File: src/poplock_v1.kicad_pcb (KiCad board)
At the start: 2 copper layers, 62 parts, among them IC1 L293D, P1 CONN_02X08, P10 CONN_02X06, P2 CONN_02X10, P3 12V Connector, P4 LOCK_CONNECTOR, P9 CONN_02X08, Q1 2n7000, Q2 2n7000, Q3 2n7000, SW1 SPST, U1 ESP-12E, U2 LD1117S50CTR, U3 LD1117S33CTR, U4 MIC_ELECTRET

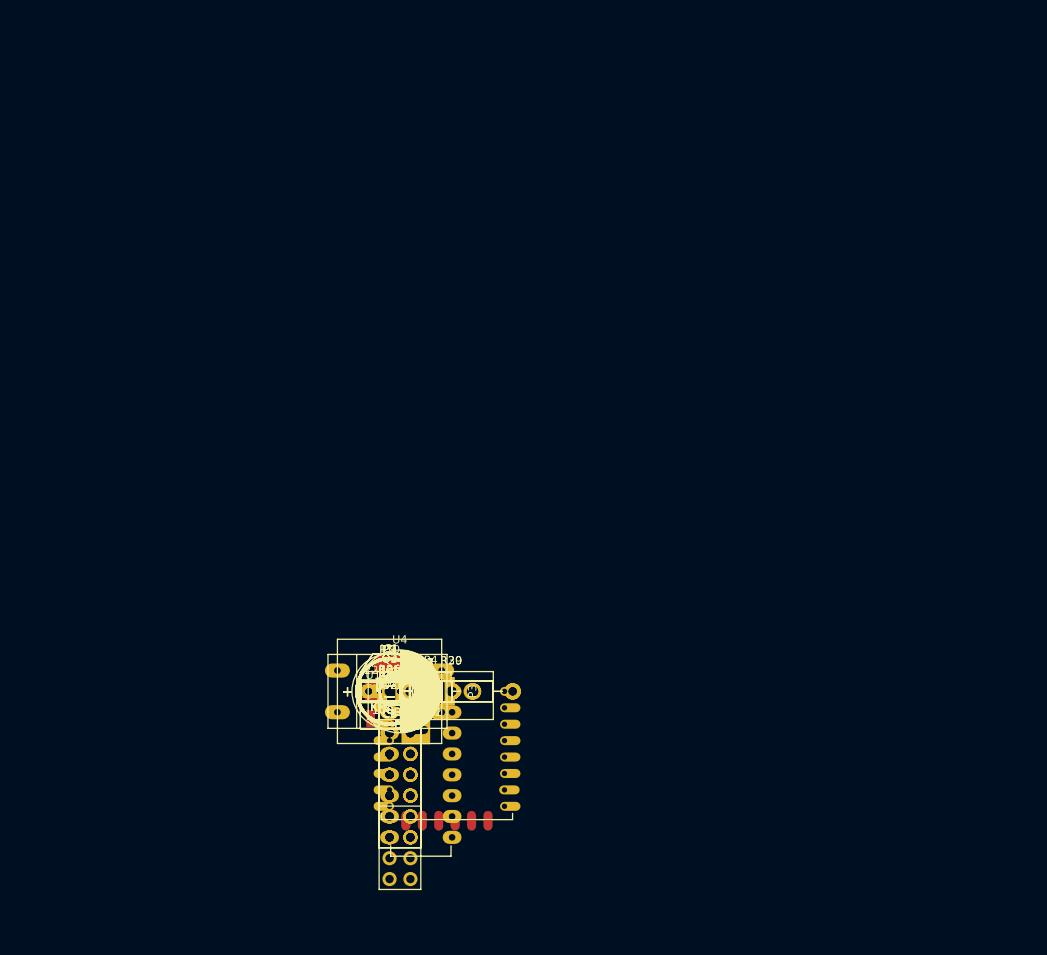
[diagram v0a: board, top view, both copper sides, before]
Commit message: Distribuidos os componentes sobre a placa.
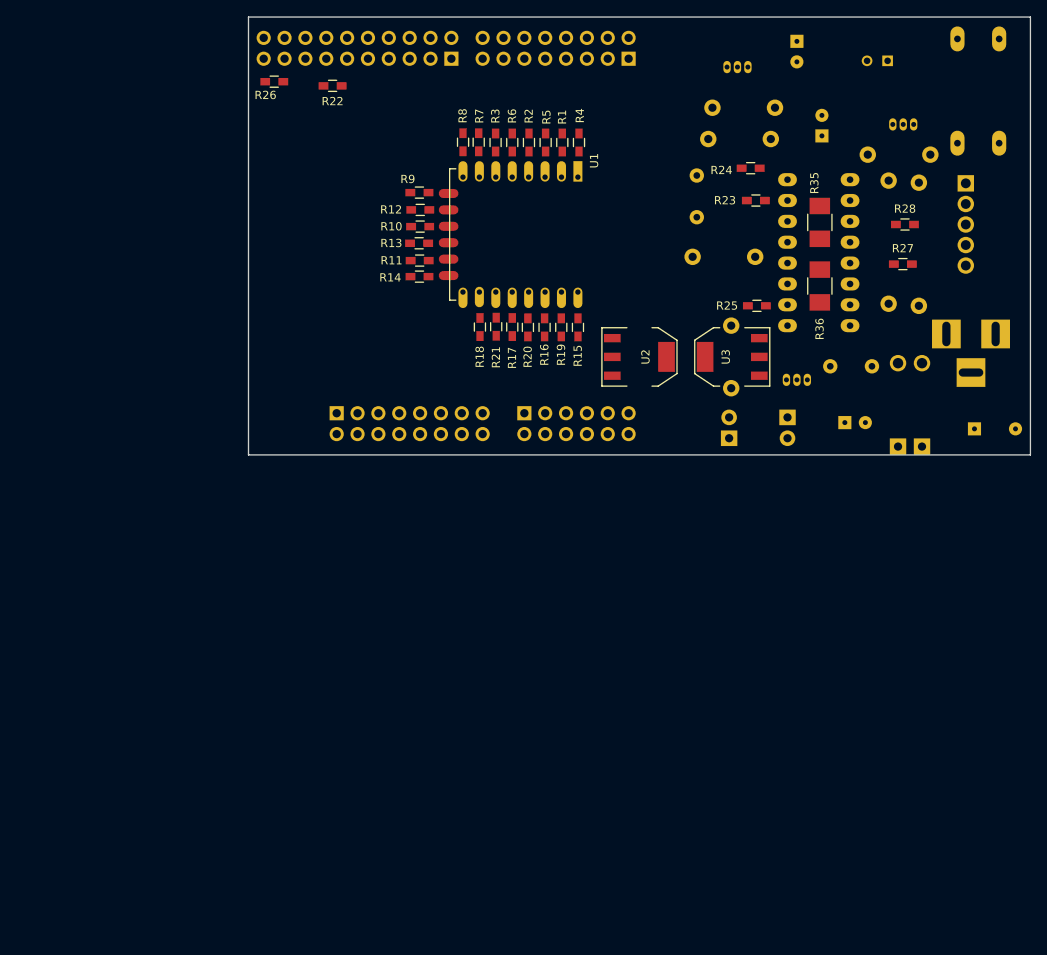
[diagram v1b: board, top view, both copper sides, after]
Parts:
- C1, C2, C3, C4, C5, C6, D1, D2, D3, D4, IC1, P1, P10, P2, P3, P9, Q1, Q2, Q3, R29, R30, R31, R32, R33, R34, R37, SW1, U4: moved to B.Cu
- P4: footprint Connect:Wafer_Vertical15x5.8x7RM2.5-5 -> Connect:Wafer_Horizontal15x5.8x7RM2.5-5; moved to B.Cu
- moved SW1 102.4 mm to (220.2, 31.9), turned to 90 degrees
- moved U4 97.9 mm to (209.2, 28.2), turned to 180 degrees
- moved Q3 94.1 mm to (212.3, 35.9), turned to 180 degrees
- moved P4 93.6 mm to (218.7, 43.1), turned to 270 degrees
- moved C6 92.4 mm to (198.1, 27.1), turned to 270 degrees
- moved R30 89.4 mm to (213.0, 43.0), turned to 270 degrees
- moved Q1 87.7 mm to (192.2, 29.0), turned to 180 degrees
- moved R33 87.6 mm to (206.8, 39.6)
- moved C3 86.7 mm to (201.2, 36.1), turned to 90 degrees
- moved P3 85.9 mm to (222.5, 61.5), turned to 180 degrees
- moved R28 84.7 mm to (211.3, 48.1)
- moved IC1 83.9 mm to (204.6, 42.7), turned to 180 degrees
- moved P1 82.4 mm to (177.6, 27.9), turned to 90 degrees
- moved R34 81.8 mm to (194.9, 37.7), turned to 180 degrees
- moved R27 81.4 mm to (211.0, 53.0)
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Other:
- board outline added: 95.2 x 53.3 mm
- net class Default: clearance 0.2 -> 0.4; trace_width 0.25 -> 0.4
- net class Power12 added: clearance 0.4, trace_width 0.4, via_dia 0.6, via_drill 0.4
- rule trace_clearance: 0.2 -> 0.4

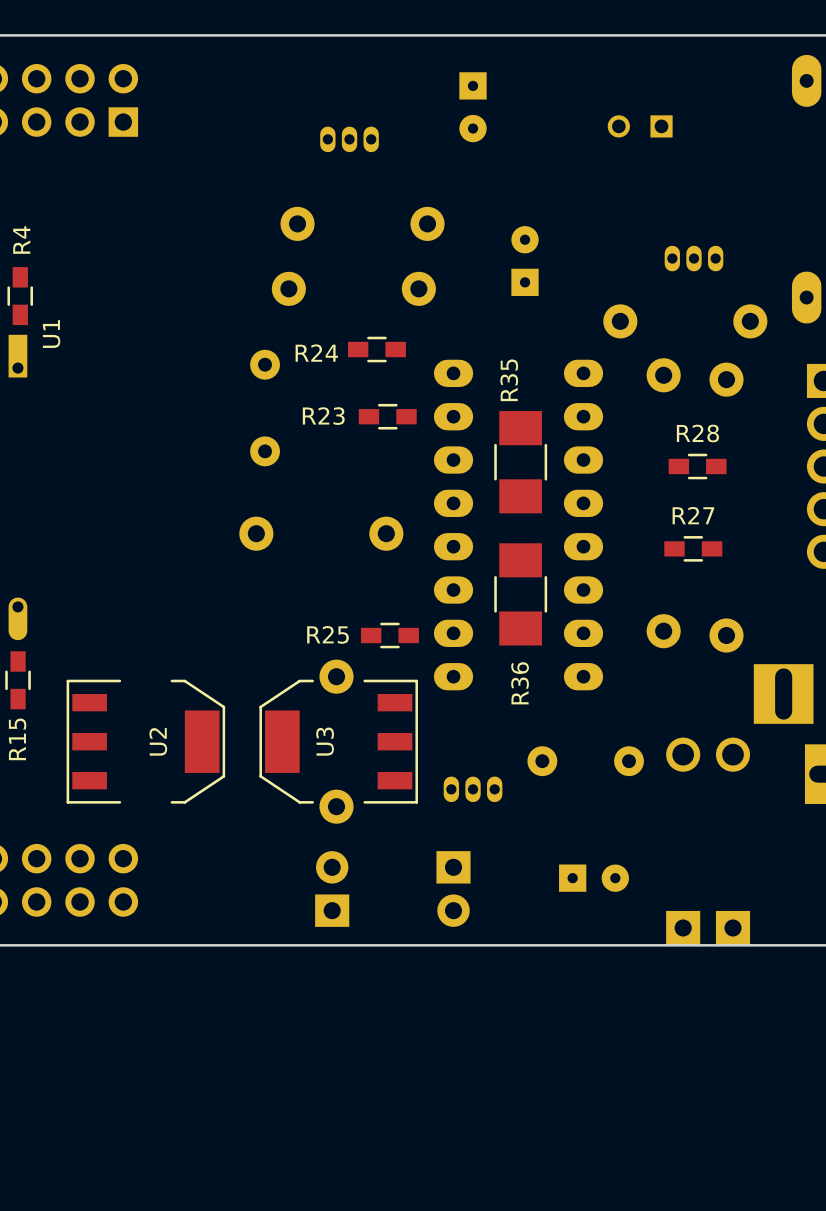
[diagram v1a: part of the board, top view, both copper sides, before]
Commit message: Removi circuito de microfone e coloquei conector de 6 pinos, além de um resistor para proteção. O conector pode ser invertido sem problemas de danos à placa. Há um novo projeto dentro da pasta placa_microfone, referente à placa externa de captura do microfone a ser conectada.
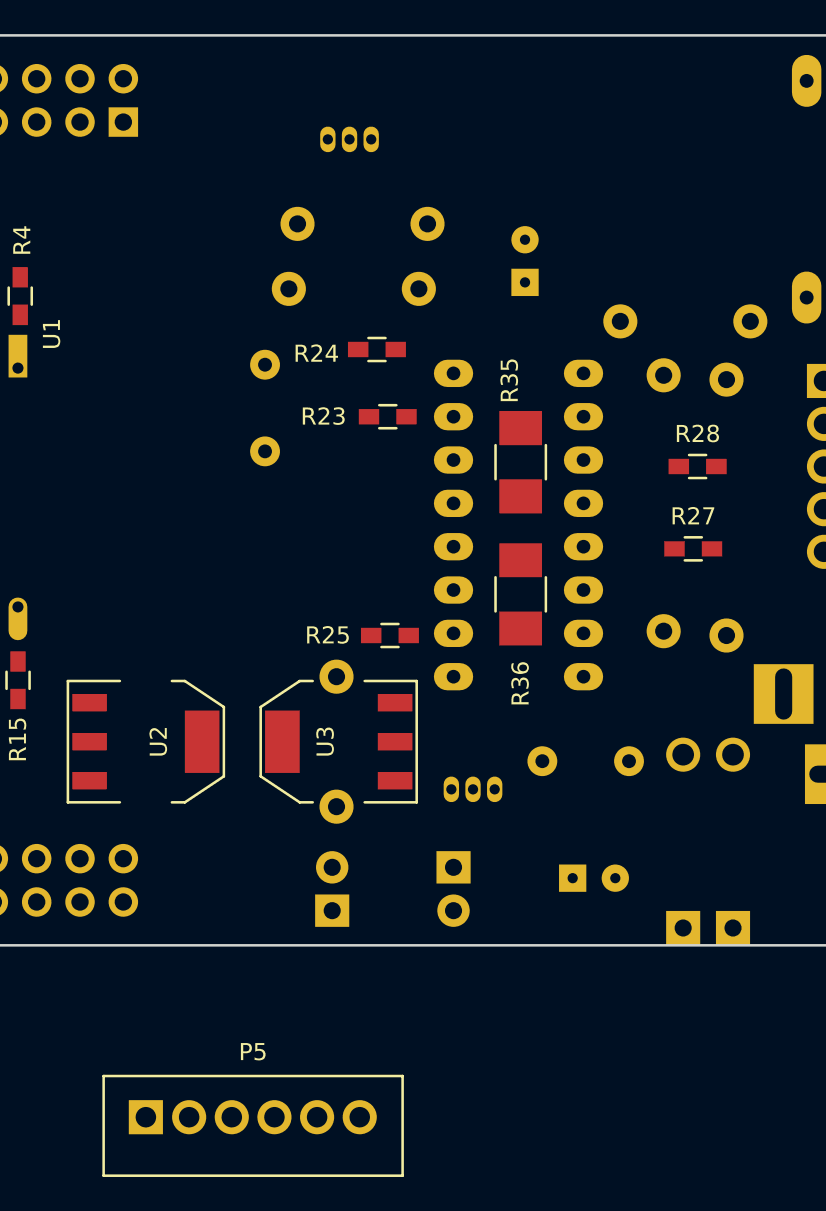
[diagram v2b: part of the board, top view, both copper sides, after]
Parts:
- removed C6: 10u, Capacitores:Cap_Eletrolitico_8x3.5
- removed Q3: 2n7000, TO_SOT_Packages_THT:TO-92_Inline_Narrow_Oval
- removed R37: 1k, Resistors_ThroughHole:Resistor_Horizontal_RM7mm
- removed U4: MIC_ELECTRET, Capacitors_ThroughHole:C_Radial_D10_L20_P2.5
- added P5: CONN_01X06, Connect:Wafer_Vertical17.5x5.8x7RM2.5-6, F.Cu at (178.9, 86.3)
- R34: value 10000 -> 150
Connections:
- R34 pad 1: +12V -> /Microfone/MIC_ANALOG_OUT

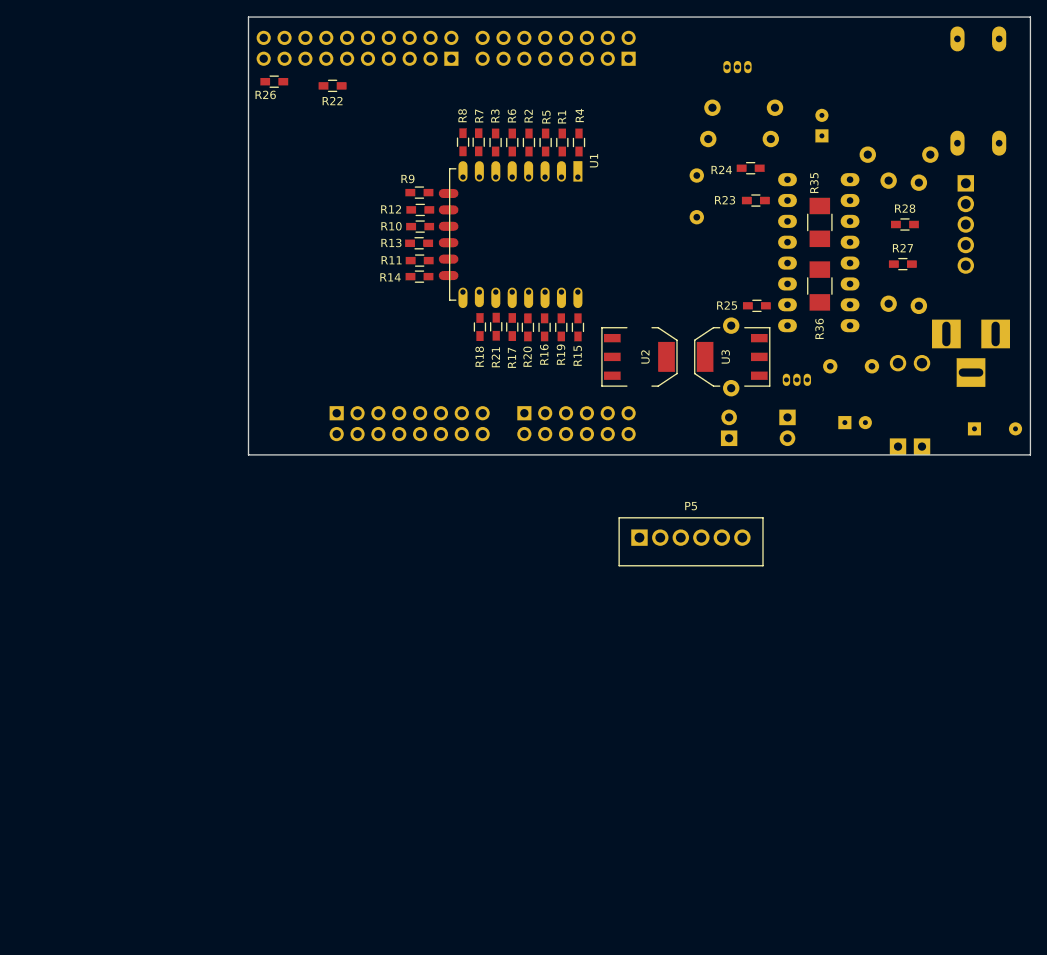
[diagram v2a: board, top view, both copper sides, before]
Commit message: PCB completa, feita a primeira revisão.
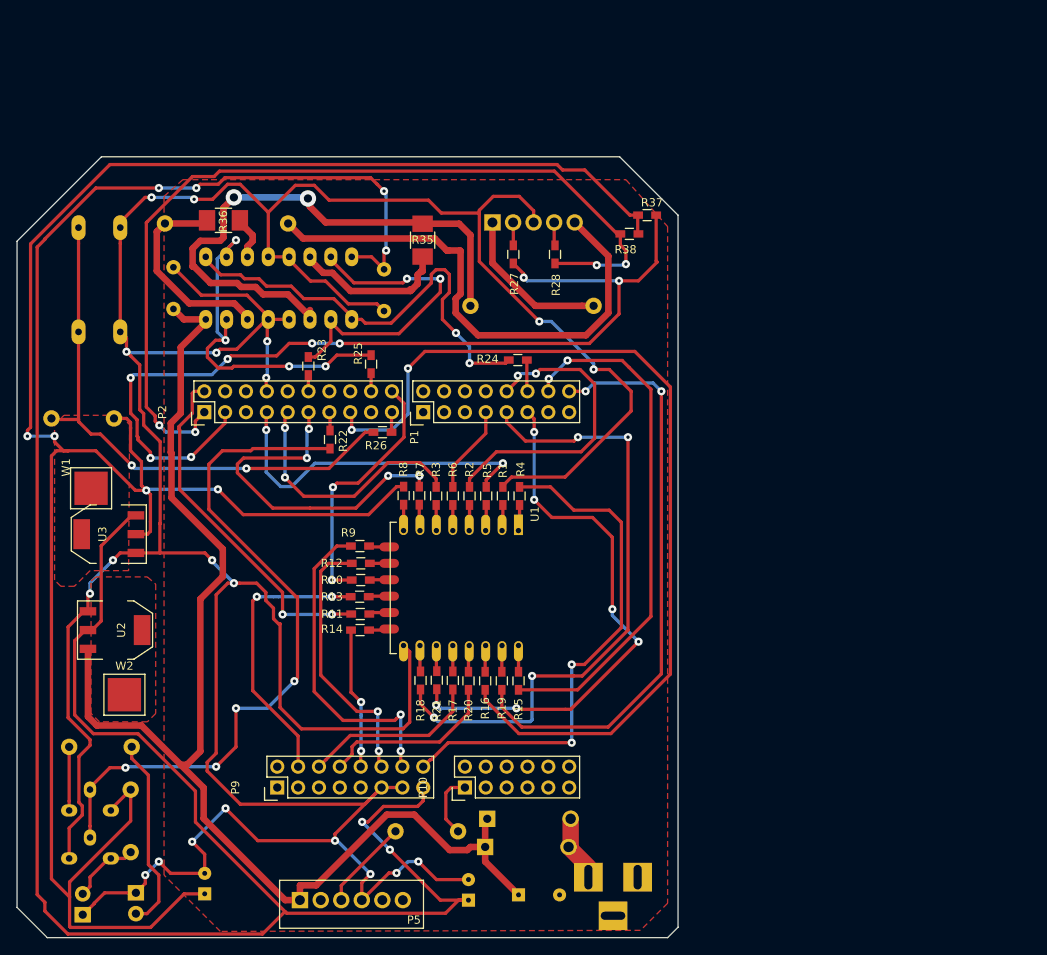
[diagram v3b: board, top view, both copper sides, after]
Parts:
- added R37: 10k, Resistors_SMD:R_0603_HandSoldering, F.Cu at (179.9, 47.0)
- added R38: 10k, Resistors_SMD:R_0603_HandSoldering, F.Cu at (177.7, 49.3)
- added W1: TEST_1P, SMD_Packages:1Pin, F.Cu at (112.1, 80.3)
- added W2: TEST_1P, SMD_Packages:1Pin, F.Cu at (116.2, 105.4)
- P1, P10, P2, P9: moved to F.Cu
- Q1, Q2: footprint TO_SOT_Packages_THT:TO-92_Inline_Narrow_Oval -> TO_SOT_Packages_THT:TO-92_Molded_Wide_Oval
- R27, R28: value 0R -> 100R
- moved Q1 119.3 mm to (114.6, 119.5)
- moved C3 119.1 mm to (126.0, 128.4)
- moved R31 110.5 mm to (109.5, 111.8)
- moved SW1 109.5 mm to (113.2, 54.9)
- moved Q2 102.9 mm to (114.6, 125.3)
- moved D3 98.3 mm to (117.6, 129.5)
- moved D4 97.8 mm to (111.1, 132.2)
- moved R33 97.3 mm to (114.9, 71.8), turned to 180 degrees
- moved R34 92.5 mm to (156.8, 122.0)
- moved R32 92.4 mm to (117.0, 117.0)
- moved C4 83.1 mm to (122.2, 55.9), turned to 90 degrees
- moved C1 79.4 mm to (166.7, 129.8)
- moved P3 79.2 mm to (178.9, 127.6)
- moved U3 79.0 mm to (114.3, 85.9)
- moved R30 77.0 mm to (136.1, 48.0), turned to 180 degrees
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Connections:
- U2 pad 4: (no net) -> /Fonte 12V/5V/3V3/DISSIPU2
- U3 pad 4: (no net) -> /Fonte 12V/5V/3V3/DISSIPU3
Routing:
- net GND: track 0.00 -> 456.1 mm, vias 0 -> 20
- net +5V: track 0.00 -> 289.7 mm, vias 0 -> 6
- net +3V3: track 0.00 -> 275.6 mm, vias 0 -> 4
- net +12V: track 0.00 -> 152.2 mm
- net /PTD6: track 0.00 -> 115.1 mm, vias 0 -> 8
- net /PTC16: track 0.00 -> 113.5 mm, vias 0 -> 2
- net /PTD7: track 0.00 -> 109.6 mm, vias 0 -> 4
- net /Interface/LOCKED_SIGNAL: track 0.00 -> 85.8 mm, vias 0 -> 4
- net /PTC4: track 0.00 -> 76.5 mm, vias 0 -> 4
- net /PTA2: track 0.00 -> 71.7 mm, vias 0 -> 2
- net Net-(IC1-Pad3): track 0.00 -> 70.0 mm, vias 0 -> 2
- net /Interface/_REQUEST_UNLOCK: track 0.00 -> 67.3 mm, vias 0 -> 2
- net /PTC3: track 0.00 -> 66.8 mm, vias 0 -> 6
- net /Trava/PhaseL: track 0.00 -> 64.0 mm
- net /PTA1: track 0.00 -> 63.9 mm, vias 0 -> 2
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- added copper zone on F.Cu, net /Fonte 12V/5V/3V3/DISSIPU2
- added copper zone on F.Cu, net /Fonte 12V/5V/3V3/DISSIPU3
- added copper zone on F.Cu, net GND
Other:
- board size 95.2 x 53.3 mm -> 80.5 x 95.1 mm
- net class Default: via_dia 0.6 -> 1
- net class Power12: trace_width 0.4 -> 0.8; via_dia 0.6 -> 2; via_drill 0.4 -> 1

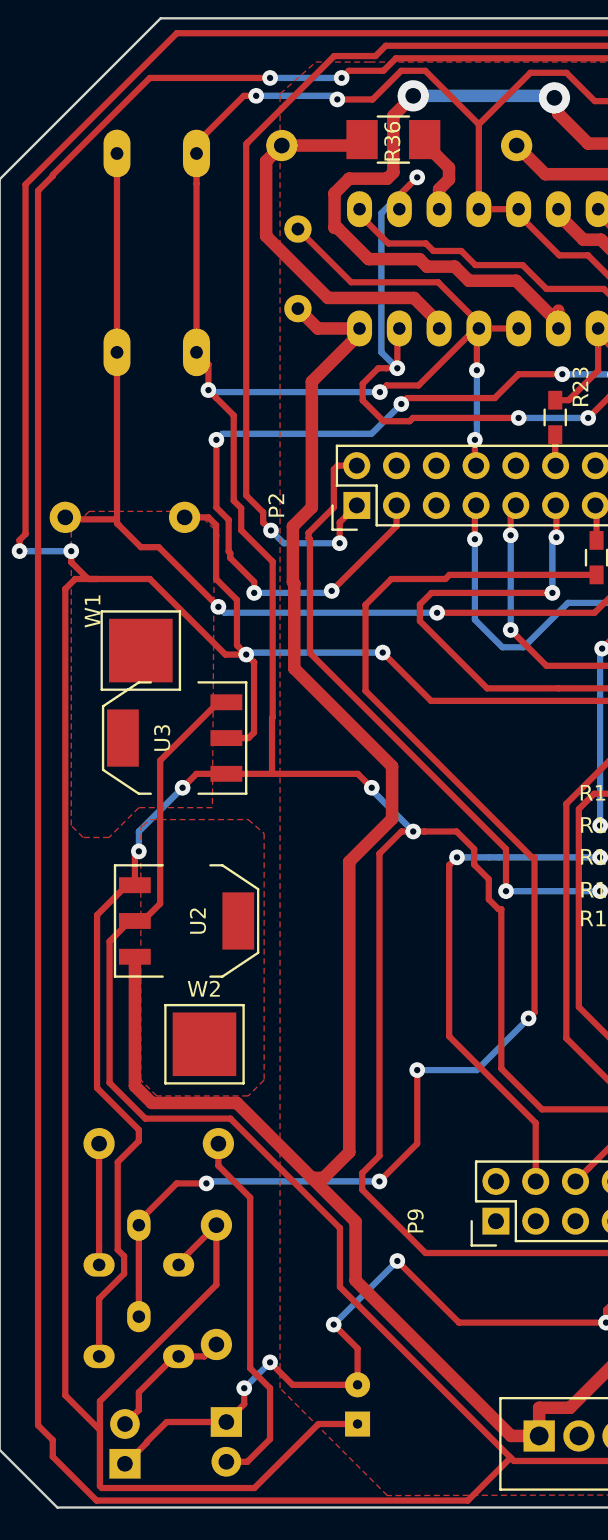
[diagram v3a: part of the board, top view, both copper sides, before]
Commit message: Modificacao footprint regulador 5v
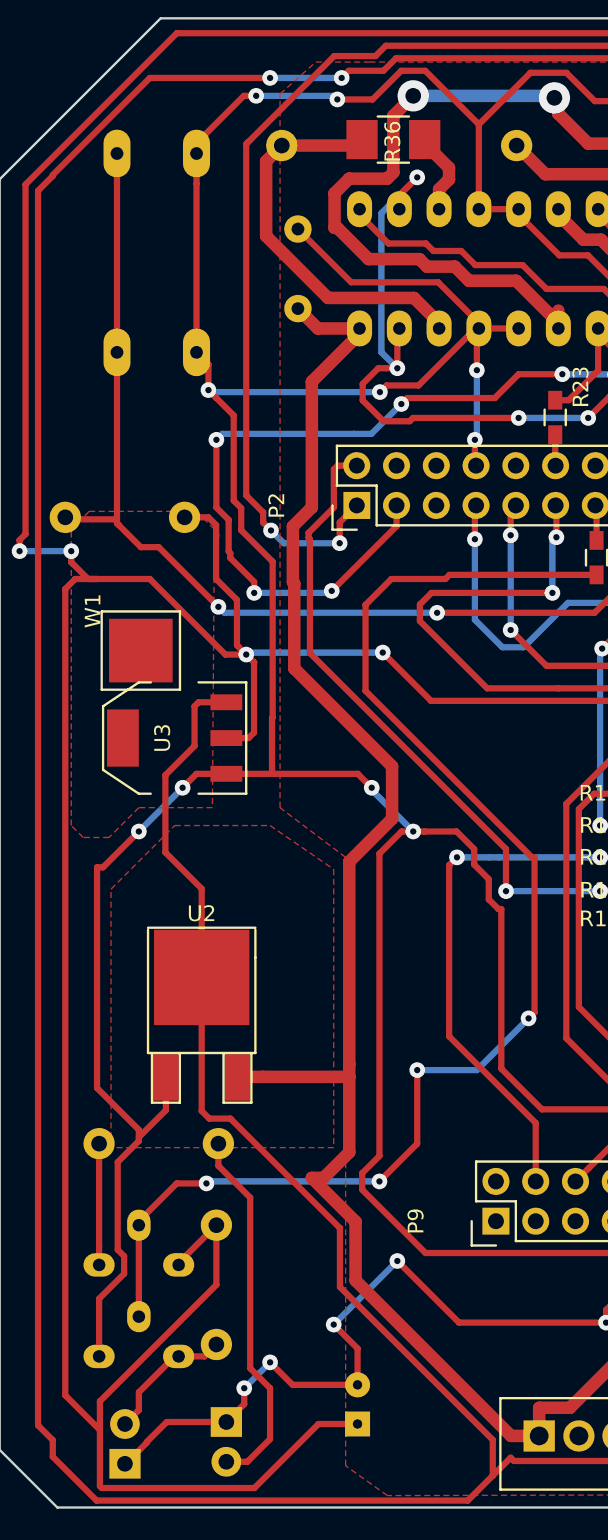
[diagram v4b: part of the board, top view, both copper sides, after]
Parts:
- removed W2: TEST_1P, SMD_Packages:1Pin
- U2: footprint TO_SOT_Packages_SMD:SOT-223 -> TO_SOT_Packages_SMD:TO-252-2Lead
- moved U2 10.0 mm to (116.0, 107.5), turned to 0 degrees
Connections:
- net /Microfone/MIC_ANALOG_OUT renamed /PTB0
- U3 pad 4: /Fonte 12V/5V/3V3/DISSIPU3 -> (no net)
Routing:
- net +12V: track 152.2 -> 137.3 mm
- net GND: track 456.1 -> 460.6 mm
- net +5V: track 289.7 -> 285.8 mm
- added copper zone on F.Cu, net +5V
- removed copper zone on F.Cu, net /Fonte 12V/5V/3V3/DISSIPU2
